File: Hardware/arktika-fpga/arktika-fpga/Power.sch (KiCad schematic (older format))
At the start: 45 parts

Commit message: Addded new hybrid crystal footprint, fixed missing footprints, created layout file for testing
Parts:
- CCP5_2, CIN1, CP10_1, CP10_2, CP1_1, CP1_2, CP1_3, CP2_1, CP2_2, CP2_3, CP3_1, CP3_2, CP3_3, CP4_1, CP4_2, CP4_3, CP5_1, CP5_3, CP6, CP6_1, CP6_2, CP6_3, CP7, CP8, CP9_1, CP9_2: footprint Capacitors_SMD:C_0603 -> Capacitors_SMD:C_0603_HandSoldering
- DP1, DP2: footprint (none) -> Diodes_SMD:D_SMA-SMB_Universal_Handsoldering
- DP3: footprint (none) -> LEDs:LED_0603_HandSoldering
- DUSB1: footprint Package_TO_SOT_SMD:SOT-143 -> TO_SOT_Packages_SMD:SOT-143
- FP1, FUSB1: footprint (none) -> Fuses:Fuse_1812_4532Metric
- JIN1: renamed from JP1; footprint (none) -> Connectors:Barrel_Jack_CUI_PJ-102AH
- JP1: footprint (none) -> Pin_Headers:Pin_Header_Straight_1x03_Pitch2.54mm
- JP2: footprint (none) -> Jumper:SolderJumper-2_P1.3mm_Open_TrianglePad1.0x1.5mm
- LP1_1, LP1_2, LP1_3: value Ferrite -> BLM31B601S; footprint (none) -> Inductors_SMD:L_1206_HandSoldering
- RP1_1, RP1_2, RP2: footprint Resistors_SMD:R_0603 -> Resistors_SMD:R_0603_HandSoldering
- UP1: footprint Package_TO_SOT_SMD:SOT-223-3_TabPin2 -> TO_SOT_Packages_SMD:SOT-223-3_TabPin2
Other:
- note added: "1812 fuse footprint\n"

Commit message: Misc schematic changes. Preliminary layout almost complete
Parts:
- removed CP6: 10n, Capacitors_SMD:C_0603_HandSoldering, symbol Device:C
- removed JP1: Conn_01x03, Pin_Headers:Pin_Header_Straight_1x03_Pitch2.54mm, symbol Connector_Generic:Conn_01x03
- added CP7_1, CP7_2, CP7_3: 10n, Capacitor_SMD:C_0603_1608Metric_Pad1.05x0.95mm_HandSolder, symbol arktika-fpga-rescue:C-Device
- CCP5_2, CP1_1, CP1_2, CP1_3, CP2_1, CP2_2, CP2_3, CP3_1, CP3_2, CP3_3, CP4_1, CP4_2, CP4_3, CP5_1, CP5_3, CP6_1, CP6_2, CP6_3: footprint Capacitors_SMD:C_0603_HandSoldering -> Capacitor_SMD:C_0603_1608Metric_Pad1.05x0.95mm_HandSolder; symbol Device:C -> arktika-fpga-rescue:C-Device
- CIN1: footprint Capacitors_SMD:C_0603_HandSoldering -> Capacitor_SMD:C_0603_1608Metric_Pad1.05x0.95mm_HandSolder; symbol Device:CP -> arktika-fpga-rescue:CP-Device
- CP10_1: renamed from CP9_1; footprint Capacitors_SMD:C_0603_HandSoldering -> Capacitor_SMD:C_0603_1608Metric_Pad1.05x0.95mm_HandSolder; symbol Device:C -> arktika-fpga-rescue:C-Device
- CP10_2: renamed from CP10_1; footprint Capacitors_SMD:C_0603_HandSoldering -> Capacitor_SMD:C_0603_1608Metric_Pad1.05x0.95mm_HandSolder; symbol Device:C -> arktika-fpga-rescue:C-Device
- CP11_1: renamed from CP9_2; footprint Capacitors_SMD:C_0603_HandSoldering -> Capacitor_SMD:C_0603_1608Metric_Pad1.05x0.95mm_HandSolder; symbol Device:C -> arktika-fpga-rescue:C-Device
- CP11_2: renamed from CP10_2; footprint Capacitors_SMD:C_0603_HandSoldering -> Capacitor_SMD:C_0603_1608Metric_Pad1.05x0.95mm_HandSolder; symbol Device:C -> arktika-fpga-rescue:C-Device
- CP8: renamed from CP7; footprint Capacitors_SMD:C_0603_HandSoldering -> Capacitor_SMD:C_0603_1608Metric_Pad1.05x0.95mm_HandSolder; symbol Device:C -> arktika-fpga-rescue:C-Device
- CP9: renamed from CP8; footprint Capacitors_SMD:C_0603_HandSoldering -> Capacitor_SMD:C_0603_1608Metric_Pad1.05x0.95mm_HandSolder; symbol Device:C -> arktika-fpga-rescue:C-Device
- DP1, DP2: footprint Diodes_SMD:D_SMA-SMB_Universal_Handsoldering -> Diode_SMD:D_SMA-SMB_Universal_Handsoldering; symbol Device:D_Schottky -> arktika-fpga-rescue:D_Schottky-Device
- DP3: footprint LEDs:LED_0603_HandSoldering -> LED_SMD:LED_0603_1608Metric_Pad1.05x0.95mm_HandSolder; symbol Device:LED -> arktika-fpga-rescue:LED-Device
- DUSB1: footprint TO_SOT_Packages_SMD:SOT-143 -> Package_TO_SOT_SMD:SOT-143; symbol Power_Protection:SP0503BAHT -> arktika-fpga-rescue:SP0503BAHT-Power_Protection
- FP1, FUSB1: footprint Fuses:Fuse_1812_4532Metric -> Fuse:Fuse_1812_4532Metric_Pad1.30x3.40mm_HandSolder; symbol Device:Fuse -> arktika-fpga-rescue:Fuse-Device
- JIN1: symbol Connector:Barrel_Jack -> arktika-fpga-rescue:Barrel_Jack-Connector
- JP2: symbol Jumper:SolderJumper_2_Open -> arktika-fpga-rescue:SolderJumper_2_Open-Jumper
- JUSB1: symbol Connector:USB_B_Micro -> arktika-fpga-rescue:USB_B_Micro-Connector
- LP1_1, LP1_2, LP1_3: footprint Inductors_SMD:L_1206_HandSoldering -> Inductor_SMD:L_1206_3216Metric_Pad1.42x1.75mm_HandSolder; symbol Device:L -> arktika-fpga-rescue:L-Device
- RP1_1, RP1_2, RP2: footprint Resistors_SMD:R_0603_HandSoldering -> Resistor_SMD:R_0603_1608Metric_Pad1.05x0.95mm_HandSolder; symbol Device:R_US -> arktika-fpga-rescue:R_US-Device
- UP1: footprint TO_SOT_Packages_SMD:SOT-223-3_TabPin2 -> Package_TO_SOT_SMD:SOT-223-3_TabPin2; symbol Regulator_Linear:AMS1117-3.3 -> arktika-fpga-rescue:AMS1117-3.3-Regulator_Linear
- UP2, UP3: footprint TO_SOT_Packages_SMD:SOT-23 -> Package_TO_SOT_SMD:SOT-23
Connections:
- wire segments 121 -> 122

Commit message: Major routing updates. Did work on silkscreen. Optimized io placing. Misc changes
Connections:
- net VCC_CORE: now also CP7_3.1
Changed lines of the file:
@@
 Connection ~ 8750 2350
 Wire Wire Line
-	8750 2350 9800 2350
+	8750 2350 9250 2350
 $Comp
 L arktika-fpga-rescue:GND-power #PWR?
@@
 $EndComp
 $Comp
-L arktika-fpga-rescue:C-Device CP7_?
-U 1 1 5F5489DE
+L arktika-fpga-rescue:C-Device CP?
+U 1 1 5F31767E
 P 9250 2500
-AR Path="/5F5489DE" Ref="CP7_?"  Part="1"
-AR Path="/5F3E98C5/5F5489DE" Ref="CP7_3"  Part="1"
+AR Path="/5F31767E" Ref="CP?"  Part="1"
+AR Path="/5F3E98C5/5F31767E" Ref="CP7_3"  Part="1"
 F 0 "CP7_3" H 9365 2546 50  0000 L CNN
 F 1 "10n" H 9365 2455 50  0000 L CNN
@@
 	-1   0    0    -1
 $EndComp
+Connection ~ 9250 2350
+Wire Wire Line
+	9250 2350 9800 2350
 $EndSCHEMATC

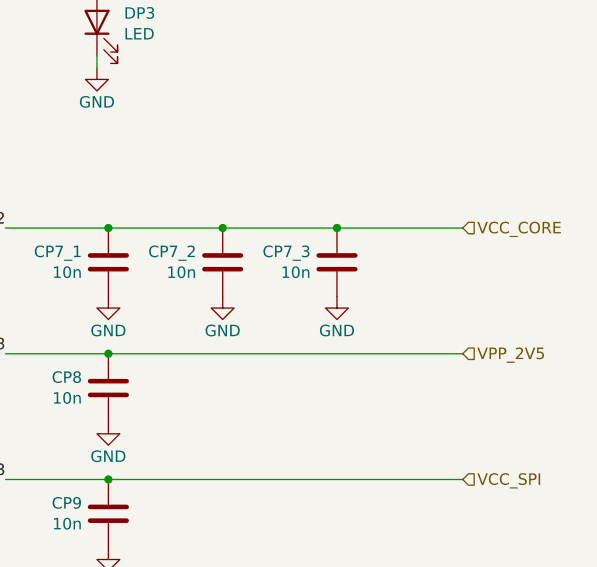
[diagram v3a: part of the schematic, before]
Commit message: Finished routing, did gnd planes, added more silkscreen and some manual via stitching. Pre-final layout.
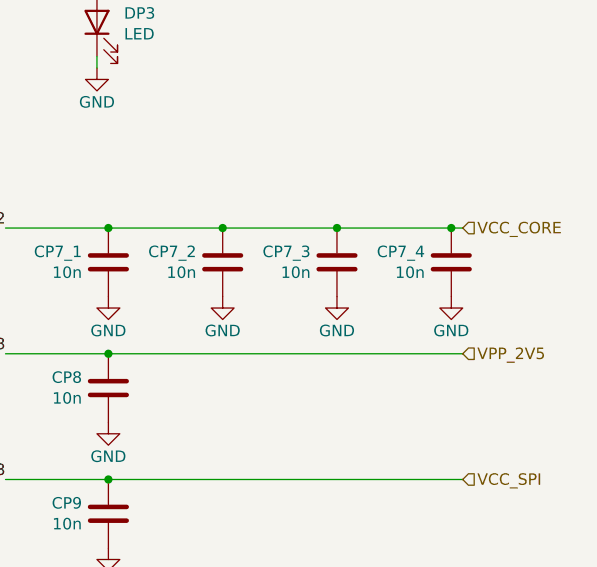
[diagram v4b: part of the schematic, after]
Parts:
- added CP7_4: 10n, Capacitor_SMD:C_0603_1608Metric_Pad1.05x0.95mm_HandSolder, symbol arktika-fpga-rescue:C-Device
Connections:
- net GND: now also CP7_4.2
- net VCC_CORE: now also CP7_4.1
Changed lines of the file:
@@
 Connection ~ 9250 2350
 Wire Wire Line
-	9250 2350 9800 2350
+	9250 2350 9750 2350
+$Comp
+L arktika-fpga-rescue:C-Device CP7_?
+U 1 1 5FDFD5F6
+P 9750 2500
+AR Path="/5FDFD5F6" Ref="CP7_?"  Part="1"
+AR Path="/5F3E98C5/5FDFD5F6" Ref="CP7_4"  Part="1"
+F 0 "CP7_4" H 9865 2546 50  0000 L CNN
+F 1 "10n" H 9865 2455 50  0000 L CNN
+F 2 "Capacitor_SMD:C_0603_1608Metric_Pad1.05x0.95mm_HandSolder" H 9788 2350 50  0001 C CNN
+F 3 "~" H 9750 2500 50  0001 C CNN
+	1    9750 2500
+	-1   0    0    -1
+$EndComp
+Connection ~ 9750 2350
+Wire Wire Line
+	9750 2350 9800 2350
+$Comp
+L arktika-fpga-rescue:GND-power #PWR?
+U 1 1 5FDFDD8F
+P 9750 2650
+AR Path="/5FDFDD8F" Ref="#PWR?"  Part="1"
+AR Path="/5F3E98C5/5FDFDD8F" Ref="#PWR?"  Part="1"
+F 0 "#PWR?" H 9750 2400 50  0001 C CNN
+F 1 "GND" H 9750 2500 50  0000 C CNN
+F 2 "" H 9750 2650 50  0001 C CNN
+F 3 "" H 9750 2650 50  0001 C CNN
+	1    9750 2650
+	-1   0    0    -1
+$EndComp
 $EndSCHEMATC

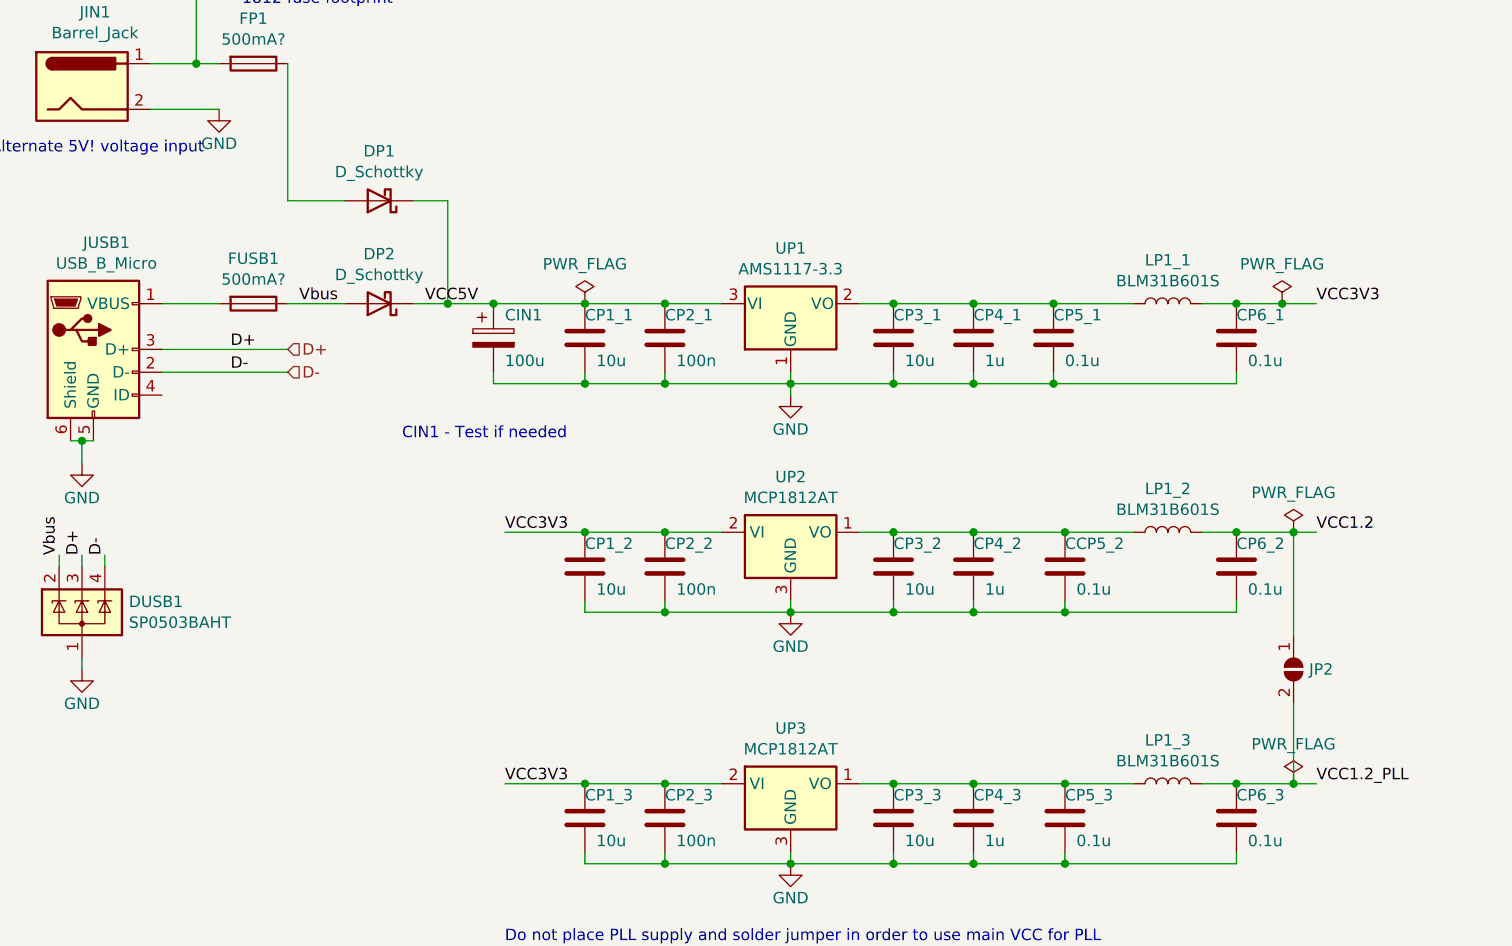
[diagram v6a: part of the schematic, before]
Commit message: Minor layout fixes. Added new micro usb connector footprint and link. Misc silk changes
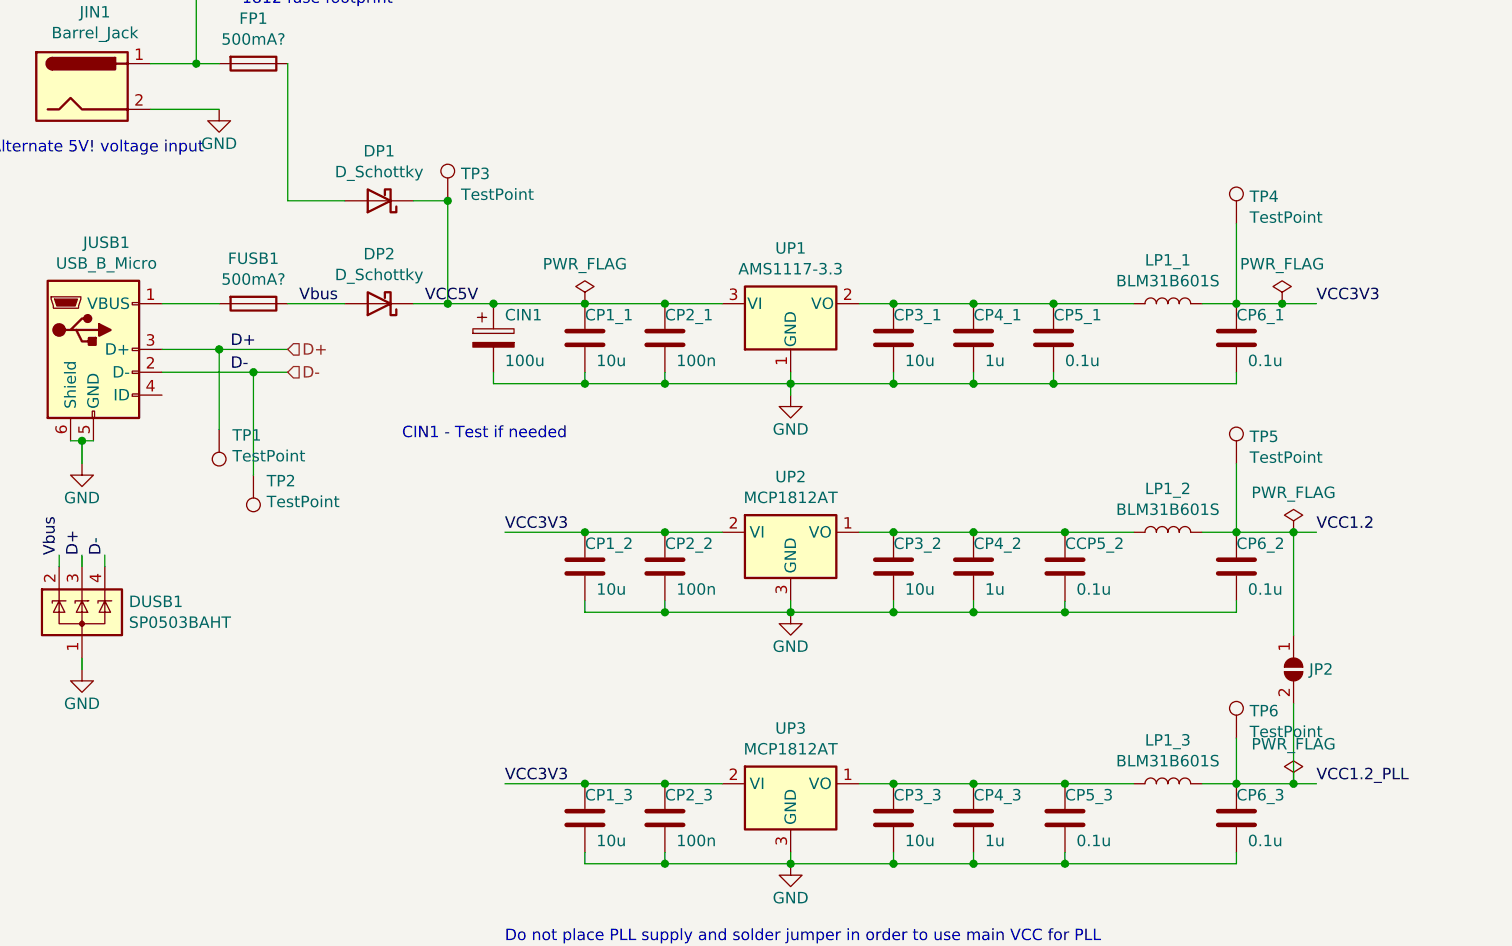
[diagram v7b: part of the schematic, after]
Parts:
- added TP1, TP2, TP3, TP4, TP5, TP6: TestPoint, Connector_Pin:Pin_D0.7mm_L6.5mm_W1.8mm_FlatFork, symbol Connector:TestPoint
- JP2: footprint Jumper:SolderJumper-2_P1.3mm_Open_TrianglePad1.0x1.5mm -> Jumper:SolderJumper-2_P1.3mm_Open_RoundedPad1.0x1.5mm
- JUSB1: footprint Connectors:USB_Micro-B -> Connector_USB:USB_Micro-B_Molex-105017-0001
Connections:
- net D+: now also TP1.1
- net D-: now also TP2.1
- net VCC1.2_PLL: now also TP6.1
- net VCC3V3: now also TP4.1
- net VCC5V: now also TP3.1
- net VCC_CORE: now also TP5.1
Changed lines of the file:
@@
 	1200 3100 1200 3200
 Wire Wire Line
-	1550 2800 2100 2800
-Wire Wire Line
-	1550 2700 2100 2700
+	1550 2800 1950 2800
+Wire Wire Line
+	1550 2700 1800 2700
 $Comp
 L arktika-fpga-rescue:Fuse-Device F?
@@
 F 0 "JUSB1" H 1307 3167 50  0000 C CNN
 F 1 "USB_B_Micro" H 1307 3076 50  0000 C CNN
-F 2 "Connectors:USB_Micro-B" H 1400 2650 50  0001 C CNN
+F 2 "Connector_USB:USB_Micro-B_Molex-105017-0001" H 1400 2650 50  0001 C CNN
 F 3 "~" H 1400 2650 50  0001 C CNN
 	1    1250 2700
@@
 F 0 "JP2" V 6500 4168 50  0000 L CNN
 F 1 "SolderJumper_2_Open" V 6545 4168 50  0001 L CNN
-F 2 "Jumper:SolderJumper-2_P1.3mm_Open_TrianglePad1.0x1.5mm" H 6500 4100 50  0001 C CNN
+F 2 "Jumper:SolderJumper-2_P1.3mm_Open_RoundedPad1.0x1.5mm" H 6500 4100 50  0001 C CNN
 F 3 "~" H 6500 4100 50  0001 C CNN
 	1    6500 4100
@@
 	-1   0    0    -1
 $EndComp
+$Comp
+L Connector:TestPoint TP3
+U 1 1 5F2CE26B
+P 2800 2050
+F 0 "TP3" H 2858 2168 50  0000 L CNN
+F 1 "TestPoint" H 2858 2077 50  0000 L CNN
+F 2 "Connector_Pin:Pin_D0.7mm_L6.5mm_W1.8mm_FlatFork" H 3000 2050 50  0001 C CNN
+F 3 "~" H 3000 2050 50  0001 C CNN
+	1    2800 2050
+	1    0    0    -1
+$EndComp
+Connection ~ 2800 2050
+$Comp
+L Connector:TestPoint TP4
+U 1 1 5F2D1406
+P 6250 2150
+F 0 "TP4" H 6308 2268 50  0000 L CNN
+F 1 "TestPoint" H 6308 2177 50  0000 L CNN
+F 2 "Connector_Pin:Pin_D0.7mm_L6.5mm_W1.8mm_FlatFork" H 6450 2150 50  0001 C CNN
+F 3 "~" H 6450 2150 50  0001 C CNN
+	1    6250 2150
+	1    0    0    -1
+$EndComp
+Wire Wire Line
+	6250 2150 6250 2500
+$Comp
+L Connector:TestPoint TP5
+U 1 1 5F2D8484
+P 6250 3200
+F 0 "TP5" H 6308 3318 50  0000 L CNN
+F 1 "TestPoint" H 6308 3227 50  0000 L CNN
+F 2 "Connector_Pin:Pin_D0.7mm_L6.5mm_W1.8mm_FlatFork" H 6450 3200 50  0001 C CNN
+F 3 "~" H 6450 3200 50  0001 C CNN
+	1    6250 3200
+	1    0    0    -1
+$EndComp
+Wire Wire Line
+	6250 3200 6250 3500
+$Comp
+L Connector:TestPoint TP6
+U 1 1 5F2DEB1D
+P 6250 4400
+F 0 "TP6" H 6308 4518 50  0000 L CNN
+F 1 "TestPoint" H 6308 4427 50  0000 L CNN
+F 2 "Connector_Pin:Pin_D0.7mm_L6.5mm_W1.8mm_FlatFork" H 6450 4400 50  0001 C CNN
+F 3 "~" H 6450 4400 50  0001 C CNN
+	1    6250 4400
+	1    0    0    -1
+$EndComp
+Wire Wire Line
+	6250 4400 6250 4600
+$Comp
+L Connector:TestPoint TP1
+U 1 1 5F302072
+P 1800 3050
+F 0 "TP1" H 1742 3076 50  0000 R CNN
+F 1 "TestPoint" H 1742 3167 50  0000 R CNN
+F 2 "Connector_Pin:Pin_D0.7mm_L6.5mm_W1.8mm_FlatFork" H 2000 3050 50  0001 C CNN
+F 3 "~" H 2000 3050 50  0001 C CNN
+	1    1800 3050
+	-1   0    0    1
+$EndComp
+$Comp
+L Connector:TestPoint TP2
+U 1 1 5F3070DB
+P 1950 3250
+F 0 "TP2" H 1892 3276 50  0000 R CNN
+F 1 "TestPoint" H 1892 3367 50  0000 R CNN
+F 2 "Connector_Pin:Pin_D0.7mm_L6.5mm_W1.8mm_FlatFork" H 2150 3250 50  0001 C CNN
+F 3 "~" H 2150 3250 50  0001 C CNN
+	1    1950 3250
+	-1   0    0    1
+$EndComp
+Wire Wire Line
+	1950 3250 1950 2800
+Connection ~ 1950 2800
+Wire Wire Line
+	1950 2800 2100 2800
+Wire Wire Line
+	1800 2700 1800 3050
+Connection ~ 1800 2700
+Wire Wire Line
+	1800 2700 2100 2700
 $EndSCHEMATC
